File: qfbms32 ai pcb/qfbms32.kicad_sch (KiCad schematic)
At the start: 17 parts, among them Q1 AGM15T03LL (CHG FET), Q2 AGM15T03LL (DSG FET), U1 BQ7695202 (IC1 - Lower 16S), U2 BQ7695202 (IC2 - Upper 16S), U3 ESP32-C3-MINI-1, U7 ISO1050 (Isolated CAN Transce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

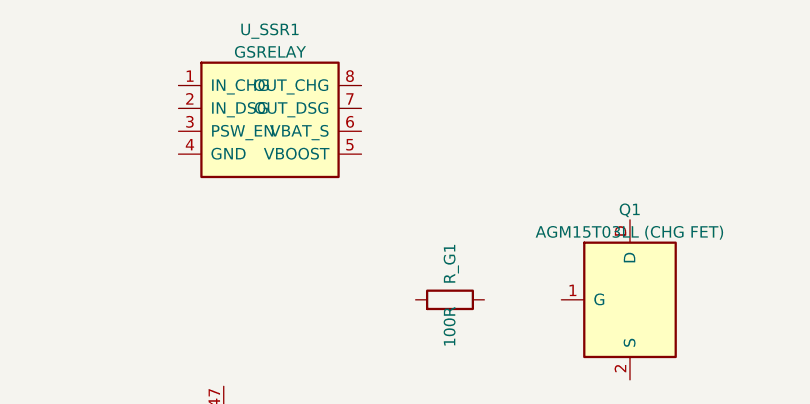
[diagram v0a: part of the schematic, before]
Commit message: feat: add qfbms32 AI PCB design files, scratch scripts, and dashboard tools
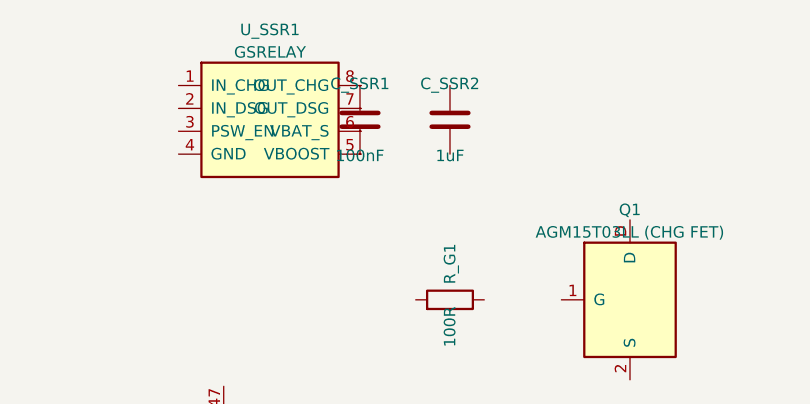
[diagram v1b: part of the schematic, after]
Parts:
- added C_SSR1: 100nF, Capacitor_SMD:C_0603_1608Metric, symbol Device:C
- added C_SSR2: 1uF, Capacitor_SMD:C_0805_2012Metric, symbol Device:C
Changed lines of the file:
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@@
+		)
+	)
+	(symbol (lib_id "Device:C")
+		(at 165.0 25.0 0)
+		(unit 1)
+		(exclude_from_sim no)
+		(in_bom yes)
+		(on_board yes)
+		(dnp no)
+		(property "Reference" "C_SSR1" (at 165.0 21.0 0) (effects (font (size 1.27 1.27))))
+		(property "Value" "100nF" (at 165.0 29.0 0) (effects (font (size 1.27 1.27))))
+		(property "Footprint" "Capacitor_SMD:C_0603_1608Metric" (at 165.0 25.0 0) (hide yes) (effects (font (size 1.27 1.27))))
+		(pin "1")
+		(pin "2")
+		(instances
+			(project "qfbms32"
+				(path "/a2322edc-ff52-449c-92df-24faffac0236" (reference "C_SSR1") (unit 1))
+			)
+		)
+	)
+	(symbol (lib_id "Device:C")
+		(at 175.0 25.0 0)
+		(unit 1)
+		(exclude_from_sim no)
+		(in_bom yes)
+		(on_board yes)
+		(dnp no)
+		(property "Reference" "C_SSR2" (at 175.0 21.0 0) (effects (font (size 1.27 1.27))))
+		(property "Value" "1uF" (at 175.0 29.0 0) (effects (font (size 1.27 1.27))))
+		(property "Footprint" "Capacitor_SMD:C_0805_2012Metric" (at 175.0 25.0 0) (hide yes) (effects (font (size 1.27 1.27))))
+		(pin "1")
+		(pin "2")
+		(instances
+			(project "qfbms32"
+				(path "/a2322edc-ff52-449c-92df-24faffac0236" (reference "C_SSR2") (unit 1))
+			)
 		)
 	)
